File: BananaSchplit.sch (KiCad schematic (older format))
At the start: 50 parts, among them J1 Screw_Terminal_01x02, J2 Screw_Terminal_01x02, J3 Screw_Terminal_01x02, J4 Screw_Terminal_01x02, Q1 AO3401A, Q2 AO3401A, U1 TPS5430DDA, U2 TPS65131RGER

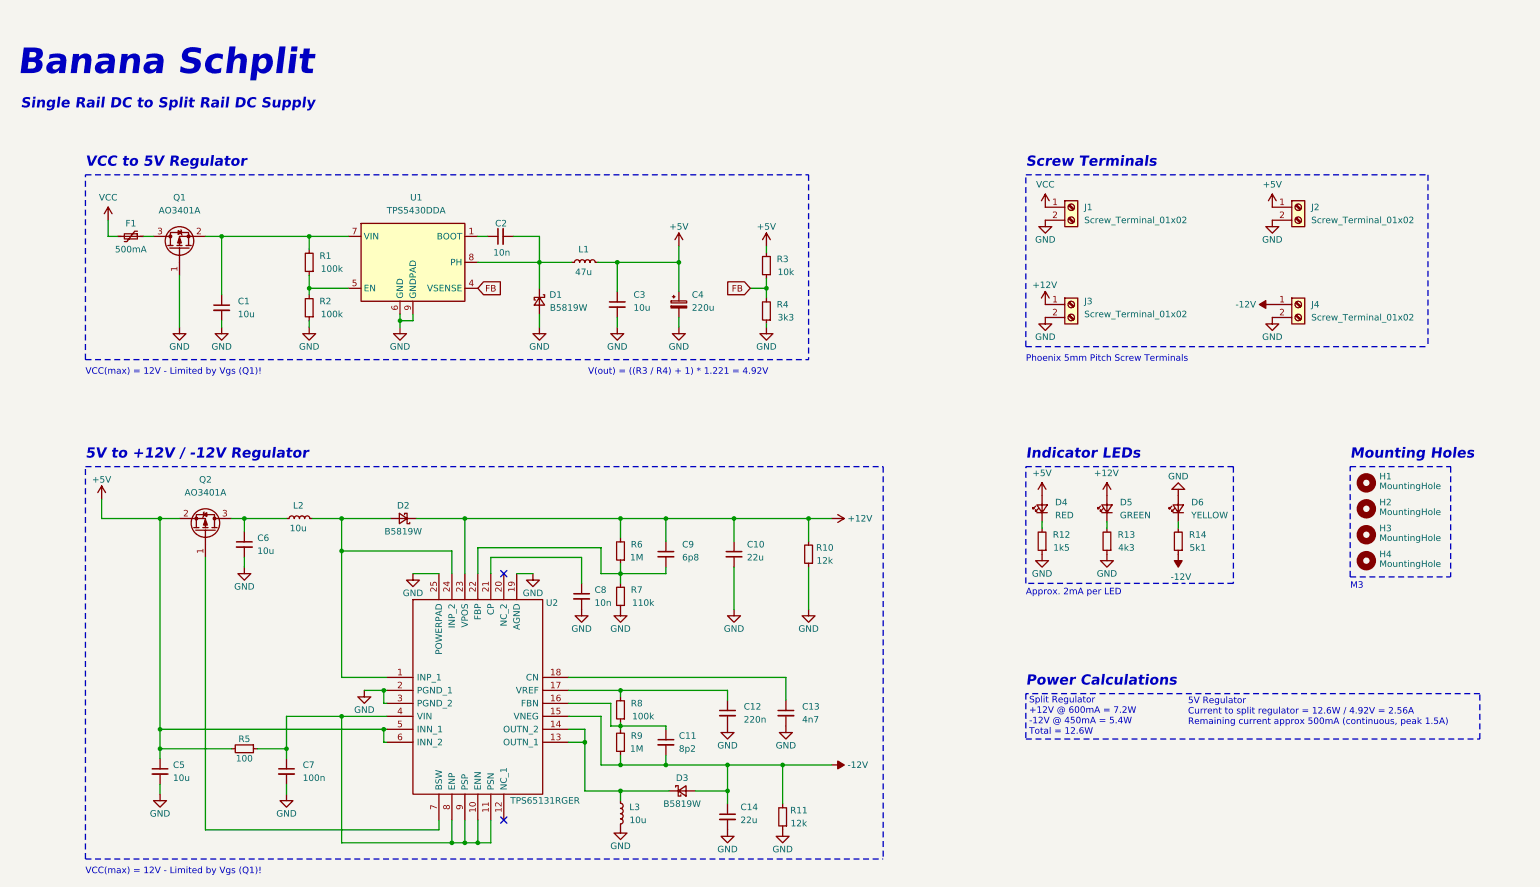
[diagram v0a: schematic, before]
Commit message: filtering + euroheaders
added more filtering/capacitance.
changed layout, added eurroack power headers and more inputs
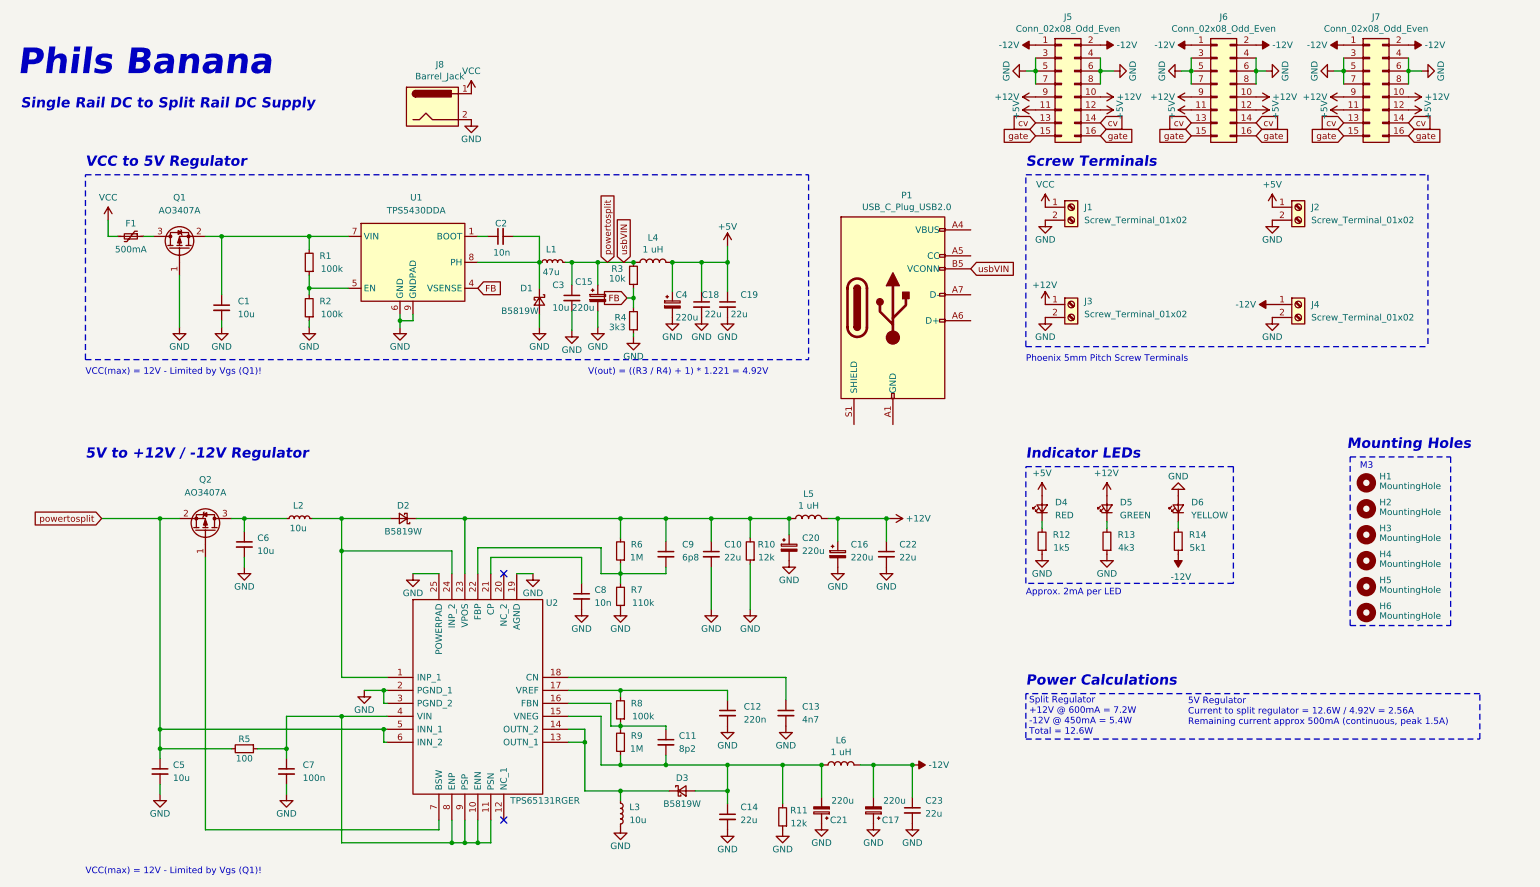
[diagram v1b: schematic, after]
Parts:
- added C15, C16, C17, C20, C21: 220u, Capacitor_SMD:CP_Elec_6.3x7.7, symbol Device:CP_Small
- added C18, C19, C22, C23: 22u, Capacitor_SMD:C_0805_2012Metric, symbol Device:C_Small
- added H5, H6: MountingHole, MountingHole:MountingHole_3.2mm_M3, symbol Mechanical:MountingHole
- added J5, J6, J7: Conn_02x08_Odd_Even, Connector_PinSocket_2.54mm:PinSocket_2x08_P2.54mm_Vertical, symbol Connector_Generic:Conn_02x08_Odd_Even
- added J8: Barrel_Jack, Connector_BarrelJack:BarrelJack_Horizontal, symbol Connector:Barrel_Jack
- added L4, L5, L6: 1 uH, BananSchplitSilk:TYS60281R0N-10, symbol Device:L
- added P1: USB_C_Plug_USB2.0, Connector_USB:USB_C_Receptacle_HRO_TYPE-C-31-M-12, symbol Connector:USB_C_Plug_USB2.0
- Q1, Q2: value AO3401A -> AO3407A; LCSC Part # C15127 -> C347478
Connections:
- net +12V: now also C16.1, C22.1, J5.10 (Pin_10), J5.9 (Pin_9), J6.10 (Pin_10), J6.9 (Pin_9), J7.10 (Pin_10), J7.9 (Pin_9), L5.2; no longer C10.1, C9.1, D2.1 (K), R10.2, R6.2, U2.23 (VPOS)
- net +5V: now also C18.1, C19.1, J5.11 (Pin_11), J5.12 (Pin_12), J6.11 (Pin_11), J6.12 (Pin_12), J7.11 (Pin_11), J7.12 (Pin_12), L4.2; no longer C3.1, C5.1, L1.2, Q2.2 (S), R3.2, R5.2, U2.5 (INN_1), U2.6 (INN_2)
- net -12V: now also C17.2, C23.1, J5.1 (Pin_1), J5.2 (Pin_2), J6.1 (Pin_1), J6.2 (Pin_2), J7.1 (Pin_1), J7.2 (Pin_2), L6.2; no longer C11.2, C14.1, D3.2 (A), R11.2, R9.1, U2.15 (VNEG)
- net GND: now also C15.2, C16.2, C17.1, C18.2, C19.2, C20.2, C21.1, C22.2, C23.2, J5.3 (Pin_3), J5.4 (Pin_4), J5.5 (Pin_5), J5.6 (Pin_6), J5.7 (Pin_7), J5.8 (Pin_8), J6.3 (Pin_3), J6.4 (Pin_4), J6.5 (Pin_5), J6.6 (Pin_6), J6.7 (Pin_7), J6.8 (Pin_8), J7.3 (Pin_3), J7.4 (Pin_4), J7.5 (Pin_5), J7.6 (Pin_6), J7.7 (Pin_7), J7.8 (Pin_8), J8.2
- net VCC: now also J8.1
- new net: C11.2, C14.1, C21.2, D3.2 (A), L6.1, R11.2, R9.1, U2.15 (VNEG)
- new net: C10.1, C20.1, C9.1, D2.1 (K), L5.1, R10.2, R6.2, U2.23 (VPOS)
- new net: P1.A1 (GND), P1.A12 (GND), P1.B1 (GND), P1.B12 (GND)
- new net: P1.A4 (VBUS), P1.A9 (VBUS), P1.B4 (VBUS), P1.B9 (VBUS)
- new net cv: J5.13 (Pin_13), J5.14 (Pin_14), J6.13 (Pin_13), J6.14 (Pin_14), J7.13 (Pin_13), J7.14 (Pin_14)
- new net gate: J5.15 (Pin_15), J5.16 (Pin_16), J6.15 (Pin_15), J6.16 (Pin_16), J7.15 (Pin_15), J7.16 (Pin_16)
- new net powertosplit: C15.1, C3.1, C5.1, L1.2, L4.1, P1.B5 (VCONN), Q2.2 (S), R3.2, R5.2, U2.5 (INN_1), U2.6 (INN_2)
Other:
- note added: "Phils Banana"
- note removed: "Banana Schplit"
- moved on the sheet: C10, C3, C4, L1, R10, R3, R4
